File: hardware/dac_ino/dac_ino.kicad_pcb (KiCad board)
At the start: 2 copper layers, 94 x 91 mm, 82 parts, among them J1 Conn_01x03_Male, J10 Conn_01x02, J11 GATE IN, J12 GATE IN, J13 GATE IN, J14 GATE IN, J15 CV IN, J16 CV IN, J17 CV IN, J18 CV IN, J2 Conn_01x03_Male, J3 Molex 2 pin, J4 Molex 2 pin, J5 Molex 2 pin, J6 Molex 2 pin, J7 VCC, J8 EURO_PWR_2x5, J9 Conn_01x04, Q1 2N3904, Q2 2N3904, Q3 2N3904, Q4 2N3904, Q5 2N3904, Q6 2N3904, U1 MCP4922, U2 TL072, U3 REF02CP+

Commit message: Late silkscreen work
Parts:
- removed the G*** at (181.6, 91.8)
- added G***: LOGO, dac_ino:deco2_dac_ino, F.Cu at (187.0, 95.5)
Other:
- board text added: "dac/ino • Rich Holmes 5/2020 • from Synapse by Vincenzo Pacella • cc-by-ca"
- board text removed: "dac/ino Vincenzo Pacella Rich Holmes 5/2020 cc-by-ca"

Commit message: Remove experimental artwork...
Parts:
- removed the G*** at (187.0, 95.5)

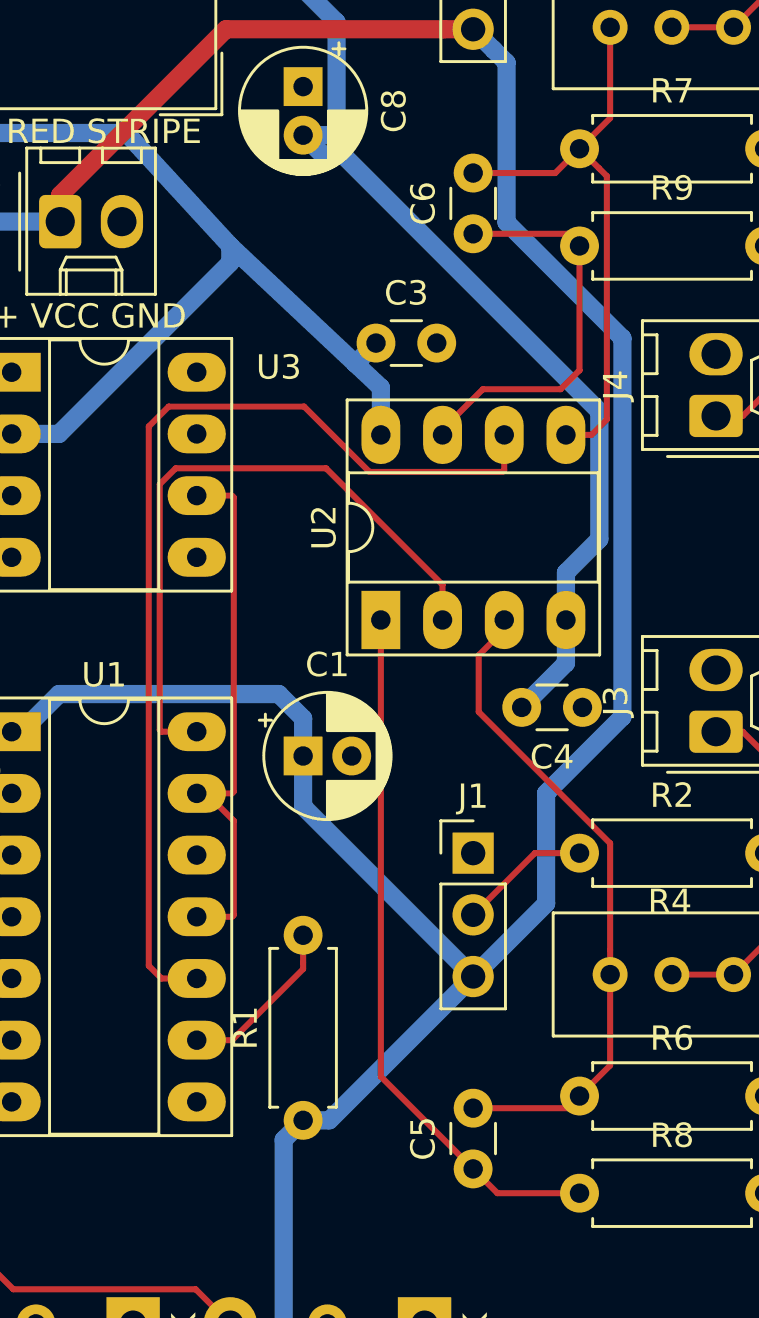
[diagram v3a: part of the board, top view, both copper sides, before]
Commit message: Correct output op amp connections
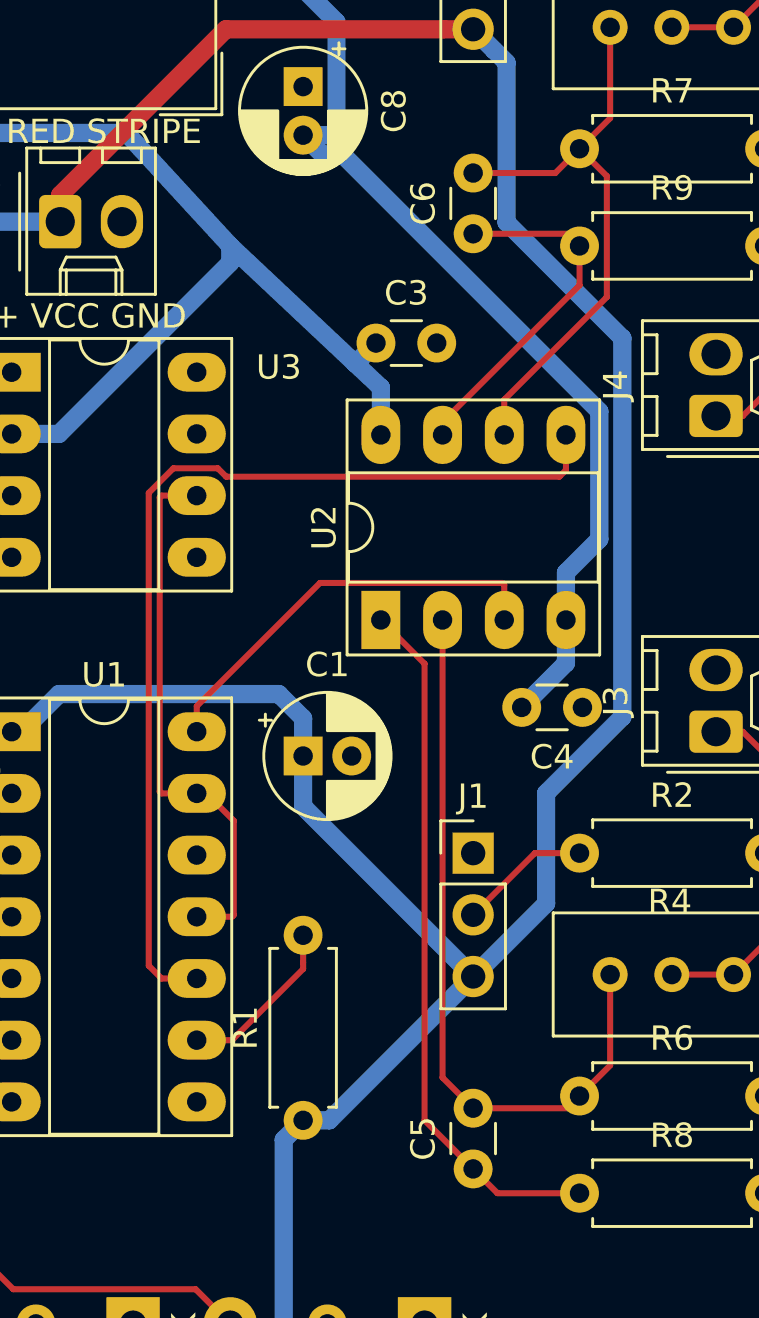
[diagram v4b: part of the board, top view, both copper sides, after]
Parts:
- J11, J12, J13, J14: value GATE IN -> Molex 2 pin GATE IN
- J15, J16, J17, J18: value CV IN -> Molex 2 pin CV IN
- J3, J4: value Molex 2 pin -> Molex 2 pin CV OUT
- J5, J6: value Molex 2 pin -> Molex 2 pin GATE OUT
- J7: value VCC -> Molex 2 pin VCC
- R1, R14: value 10K -> 10k
- R2, R3: value 91K -> 91k
- R6, R7: value 100K -> 100k
- R8, R9: value 1K -> 1k
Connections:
- U2 pad 2: /CV out/DAC_A -> Net-(C5-Pad2)
- U2 pad 3: Net-(C5-Pad2) -> /CV out/DAC_A
- U2 pad 5: Net-(C6-Pad2) -> /CV out/DAC_B
- U2 pad 6: /CV out/DAC_B -> Net-(C6-Pad2)
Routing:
- net /CV out/DAC_A: track 27.0 -> 17.7 mm
- net Net-(C5-Pad2): track 27.4 -> 30.7 mm
- net Net-(C6-Pad1): track 16.6 -> 14.7 mm
- net /CV out/DAC_B: track 42.0 -> 41.0 mm

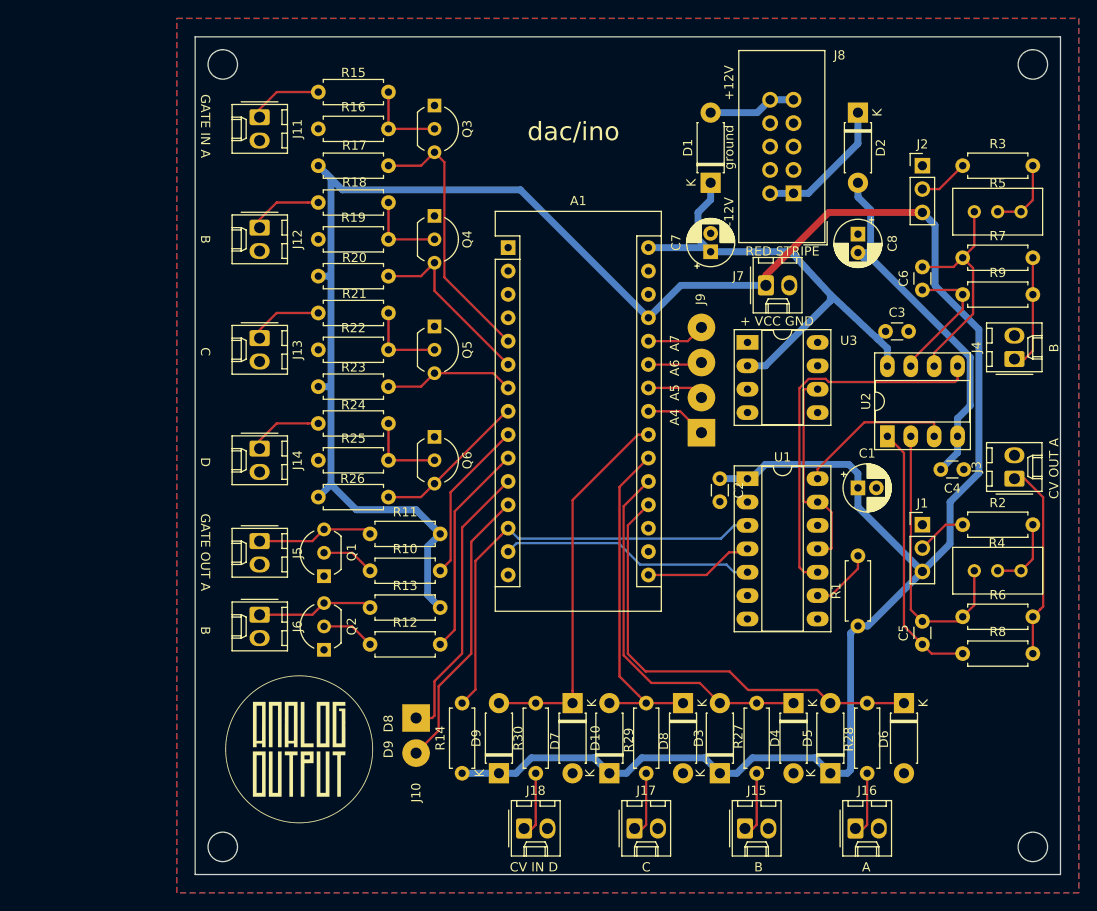
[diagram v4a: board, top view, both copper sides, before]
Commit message: Add headers for board coupling
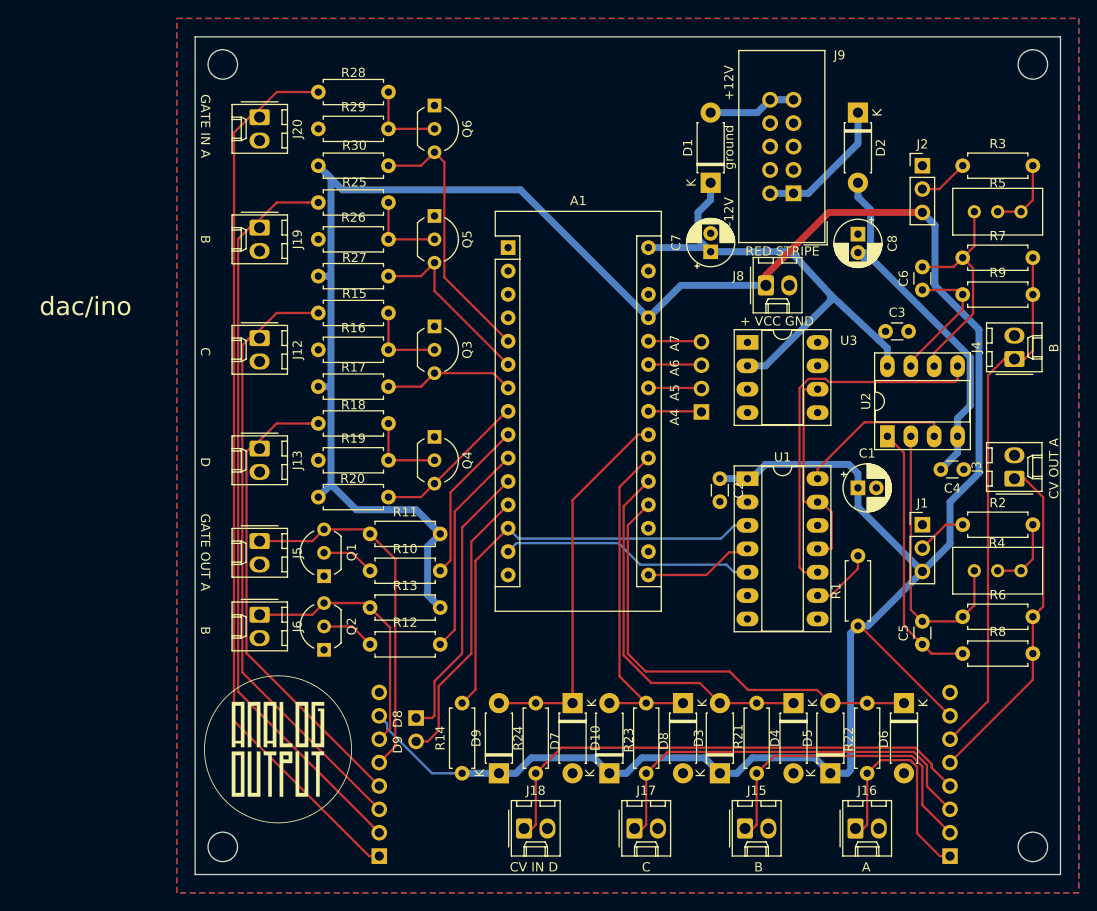
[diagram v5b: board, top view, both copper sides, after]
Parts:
- added J14: Conn_01x01_Units, Connector_PinHeader_2.54mm:PinHeader_1x08_P2.54mm_Vertical, B.Cu at (222.0, 139.0)
- added J7: Conn_01x01_Units, Connector_PinHeader_2.54mm:PinHeader_1x08_P2.54mm_Vertical, B.Cu at (160.0, 139.0)
- J10: renamed from J9; footprint Connector_Wire:SolderWirePad_1x04_P3.81mm_Drill1.2mm -> Connector_PinHeader_2.54mm:PinHeader_1x04_P2.54mm_Vertical; moved to B.Cu
- J11: renamed from J10; footprint Connector_Wire:SolderWirePad_1x02_P3.81mm_Drill1.2mm -> Connector_PinHeader_2.54mm:PinHeader_1x02_P2.54mm_Vertical; moved to B.Cu
- moved G*** 2.30 mm to (149.0, 127.4)
- moved J10 2.25 mm to (195.0, 90.8), turned to 0 degrees
- turned J11 to 180 degrees
- renumbered J13 to J12, J14 to J13, J12 to J19, J11 to J20, J7 to J8, J8 to J9, Q5 to Q3, Q6 to Q4, Q4 to Q5, Q3 to Q6, R21 to R15, R22 to R16, R23 to R17, R24 to R18, R25 to R19, R26 to R20, R27 to R21, R28 to R22, R29 to R23, R30 to R24, R18 to R25, R19 to R26, R20 to R27, R15 to R28, R16 to R29, R17 to R30
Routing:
- net /Inputs/Gate in A/GATE_IN: track 8.02 -> 97.3 mm
- net /Inputs/Gate in B/GATE_IN: track 8.02 -> 81.7 mm
- net /Inputs/Gate in C/GATE_IN: track 8.02 -> 66.8 mm
- net /Inputs/CV IN D/CV_IN: track 7.04 -> 55.1 mm
- net /CV out/CV_OUT_B: track 12.5 -> 57.3 mm
- net /Inputs/Gate in D/GATE_IN: track 8.02 -> 51.9 mm
- net /Inputs/CV in C/CV_IN: track 7.04 -> 44.9 mm
- net /Inputs/CV in B/CV_IN: track 7.04 -> 34.7 mm
- net /Gate out/GATE_OUT_A: track 12.7 -> 39.4 mm
- net VCC: track 285.0 -> 310.9 mm
- net /Inputs/CV in A/CV_IN: track 7.04 -> 25.2 mm
- net /Gate out/GATE_OUT_B: track 12.7 -> 28.4 mm
- net /CV out/CV_OUT_A: track 21.4 -> 37.0 mm
- net /Arduino/A4: track 6.72 -> 5.79 mm
- net /Arduino/A7: track 6.38 -> 5.79 mm
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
